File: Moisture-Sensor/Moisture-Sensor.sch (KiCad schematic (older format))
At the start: 18 parts, among them J1 Input, U1 LMV358, U2 NE555

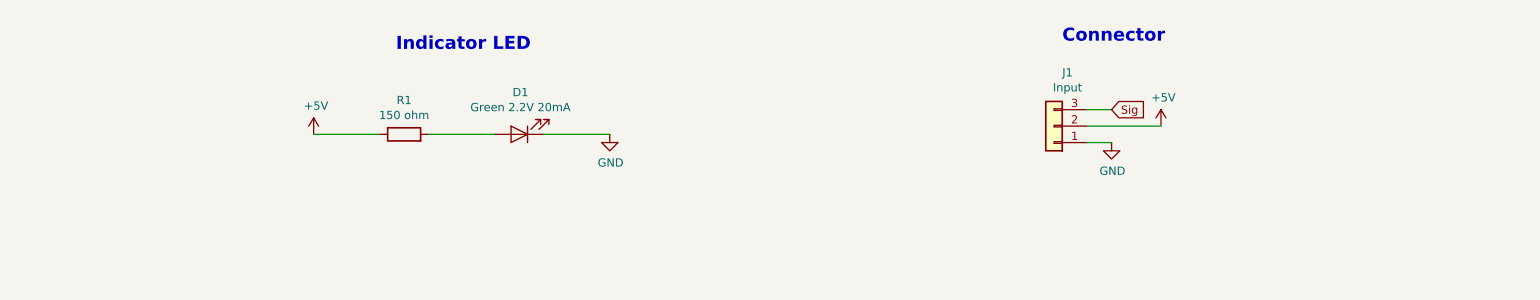
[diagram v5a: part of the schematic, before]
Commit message: Almost done routing, need to move bypass caps
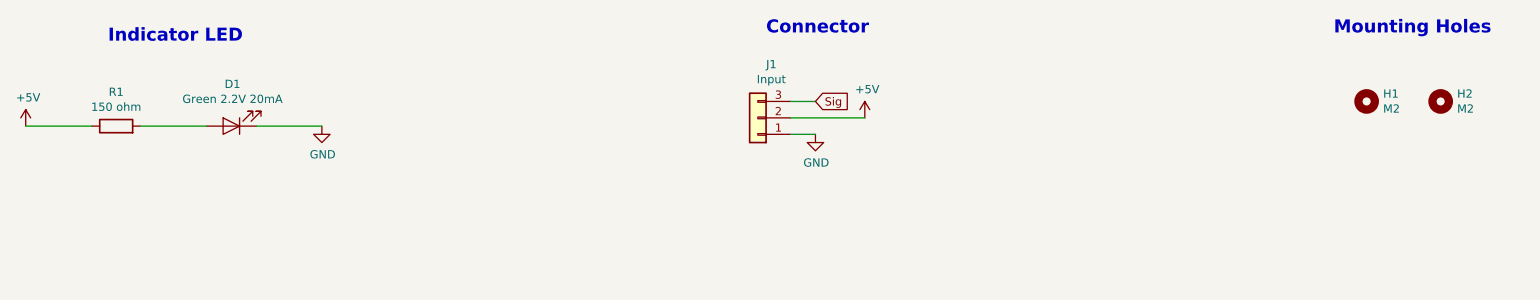
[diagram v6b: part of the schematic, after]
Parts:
- added H1, H2: M2, MountingHole:MountingHole_2.2mm_M2_ISO14580_Pad, symbol Mechanical:MountingHole
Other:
- note added: "Mounting Holes"
- moved on the sheet: D1, J1, R1
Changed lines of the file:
@@
 EESchema Schematic File Version 4
-LIBS:Moisture-Sensor-cache
 EELAYER 30 0
 EELAYER END
@@
 L Device:R R1
 U 1 1 5FE8F3C9
-P 3200 2050
-F 0 "R1" V 3407 2050 50  0000 C CNN
-F 1 "150 ohm" V 3316 2050 50  0000 C CNN
-F 2 "Resistor_SMD:R_0603_1608Metric_Pad1.05x0.95mm_HandSolder" V 3130 2050 50  0001 C CNN
-F 3 "~" H 3200 2050 50  0001 C CNN
-	1    3200 2050
+P 1450 2000
+F 0 "R1" V 1657 2000 50  0000 C CNN
+F 1 "150 ohm" V 1566 2000 50  0000 C CNN
+F 2 "Resistor_SMD:R_0603_1608Metric_Pad1.05x0.95mm_HandSolder" V 1380 2000 50  0001 C CNN
+F 3 "~" H 1450 2000 50  0001 C CNN
+	1    1450 2000
 	0    -1   -1   0
 $EndComp
@@
 L Device:LED D1
 U 1 1 5FE8F924
-P 3900 2050
-F 0 "D1" H 3893 1795 50  0000 C CNN
-F 1 "Green 2.2V 20mA" H 3893 1886 50  0000 C CNN
-F 2 "LED_SMD:LED_0603_1608Metric_Pad1.05x0.95mm_HandSolder" H 3900 2050 50  0001 C CNN
-F 3 "~" H 3900 2050 50  0001 C CNN
-	1    3900 2050
+P 2150 2000
+F 0 "D1" H 2143 1745 50  0000 C CNN
+F 1 "Green 2.2V 20mA" H 2143 1836 50  0000 C CNN
+F 2 "LED_SMD:LED_0603_1608Metric_Pad1.05x0.95mm_HandSolder" H 2150 2000 50  0001 C CNN
+F 3 "~" H 2150 2000 50  0001 C CNN
+	1    2150 2000
 	-1   0    0    1
 $EndComp
@@
 L power:GND #PWR0101
 U 1 1 5FE903CE
-P 4450 2050
-F 0 "#PWR0101" H 4450 1800 50  0001 C CNN
-F 1 "GND" H 4455 1877 50  0000 C CNN
-F 2 "" H 4450 2050 50  0001 C CNN
-F 3 "" H 4450 2050 50  0001 C CNN
-	1    4450 2050
-	1    0    0    -1
-$EndComp
-Wire Wire Line
-	2650 2050 3050 2050
-Wire Wire Line
-	3350 2050 3750 2050
-Wire Wire Line
-	4050 2050 4450 2050
+P 2700 2000
+F 0 "#PWR0101" H 2700 1750 50  0001 C CNN
+F 1 "GND" H 2705 1827 50  0000 C CNN
+F 2 "" H 2700 2000 50  0001 C CNN
+F 3 "" H 2700 2000 50  0001 C CNN
+	1    2700 2000
+	1    0    0    -1
+$EndComp
+Wire Wire Line
+	900  2000 1300 2000
+Wire Wire Line
+	1600 2000 2000 2000
+Wire Wire Line
+	2300 2000 2700 2000
 $Comp
 L Connector_Generic:Conn_01x03 J1
 U 1 1 5FE95D2E
-P 7150 2000
-F 0 "J1" H 7068 1675 50  0000 C CNN
-F 1 "Input" H 7068 1766 50  0000 C CNN
-F 2 "Connector_PinHeader_2.54mm:PinHeader_1x03_P2.54mm_Vertical" H 7150 2000 50  0001 C CNN
-F 3 "~" H 7150 2000 50  0001 C CNN
-	1    7150 2000
+P 5350 1950
+F 0 "J1" H 5268 1625 50  0000 C CNN
+F 1 "Input" H 5268 1716 50  0000 C CNN
+F 2 "Connector_PinHeader_2.54mm:PinHeader_1x03_P2.54mm_Vertical" H 5350 1950 50  0001 C CNN
+F 3 "~" H 5350 1950 50  0001 C CNN
+	1    5350 1950
 	-1   0    0    1
 $EndComp
-Text GLabel 7500 1900 2    50   Input ~ 0
+Text GLabel 5700 1850 2    50   Input ~ 0
 Sig
 $Comp
 L power:GND #PWR0102
 U 1 1 5FE9738F
-P 7500 2100
-F 0 "#PWR0102" H 7500 1850 50  0001 C CNN
-F 1 "GND" H 7505 1927 50  0000 C CNN
-F 2 "" H 7500 2100 50  0001 C CNN
-F 3 "" H 7500 2100 50  0001 C CNN
-	1    7500 2100
-	1    0    0    -1
-$EndComp
-Wire Wire Line
-	7350 1900 7500 1900
-Wire Wire Line
-	7350 2000 7800 2000
-Wire Wire Line
-	7350 2100 7500 2100
+P 5700 2050
+F 0 "#PWR0102" H 5700 1800 50  0001 C CNN
+F 1 "GND" H 5705 1877 50  0000 C CNN
+F 2 "" H 5700 2050 50  0001 C CNN
+F 3 "" H 5700 2050 50  0001 C CNN
+	1    5700 2050
+	1    0    0    -1
+$EndComp
+Wire Wire Line
+	5550 1850 5700 1850
+Wire Wire Line
+	5550 1950 6000 1950
+Wire Wire Line
+	5550 2050 5700 2050
 $Comp
 L Device:C C2
@@
 L power:+5V #PWR0103
 U 1 1 5FEC44E3
-P 7800 2000
-F 0 "#PWR0103" H 7800 1850 50  0001 C CNN
-F 1 "+5V" H 7815 2173 50  0000 C CNN
-F 2 "" H 7800 2000 50  0001 C CNN
-F 3 "" H 7800 2000 50  0001 C CNN
-	1    7800 2000
+P 6000 1950
+F 0 "#PWR0103" H 6000 1800 50  0001 C CNN
+F 1 "+5V" H 6015 2123 50  0000 C CNN
+F 2 "" H 6000 1950 50  0001 C CNN
+F 3 "" H 6000 1950 50  0001 C CNN
+	1    6000 1950
 	1    0    0    -1
 $EndComp
@@
 Wire Wire Line
 	4150 4950 4550 4950
-Text Notes 3150 1550 0    79   ~ 16
+Text Notes 1400 1500 0    79   ~ 16
 Indicator LED
 $Comp
 L power:+5V #PWR0116
 U 1 1 6000247E
-P 2650 2050
-F 0 "#PWR0116" H 2650 1900 50  0001 C CNN
-F 1 "+5V" H 2665 2223 50  0000 C CNN
-F 2 "" H 2650 2050 50  0001 C CNN
-F 3 "" H 2650 2050 50  0001 C CNN
-	1    2650 2050
-	1    0    0    -1
-$EndComp
-Text Notes 7200 1500 0    79   ~ 16
+P 900 2000
+F 0 "#PWR0116" H 900 1850 50  0001 C CNN
+F 1 "+5V" H 915 2173 50  0000 C CNN
+F 2 "" H 900 2000 50  0001 C CNN
+F 3 "" H 900 2000 50  0001 C CNN
+	1    900  2000
+	1    0    0    -1
+$EndComp
+Text Notes 5400 1450 0    79   ~ 16
 Connector
 Text Notes 3250 3200 0    79   ~ 16
@@
 Text Notes 5250 4650 0    50   ~ 0
 Capacitor Trace
+$Comp
+L Mechanical:MountingHole H1
+U 1 1 5FECF485
+P 9050 1850
+F 0 "H1" H 9150 1896 50  0000 L CNN
+F 1 "M2" H 9150 1805 50  0000 L CNN
+F 2 "MountingHole:MountingHole_2.2mm_M2_ISO14580_Pad" H 9050 1850 50  0001 C CNN
+F 3 "~" H 9050 1850 50  0001 C CNN
+	1    9050 1850
+	1    0    0    -1
+$EndComp
+$Comp
+L Mechanical:MountingHole H2
+U 1 1 5FED2177
+P 9500 1850
+F 0 "H2" H 9600 1896 50  0000 L CNN
+F 1 "M2" H 9600 1805 50  0000 L CNN
+F 2 "MountingHole:MountingHole_2.2mm_M2_ISO14580_Pad" H 9500 1850 50  0001 C CNN
+F 3 "~" H 9500 1850 50  0001 C CNN
+	1    9500 1850
+	1    0    0    -1
+$EndComp
+Text Notes 8850 1450 0    79   ~ 16
+Mounting Holes
 $EndSCHEMATC
